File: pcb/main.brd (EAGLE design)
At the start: 100 x 80 mm, 1 part

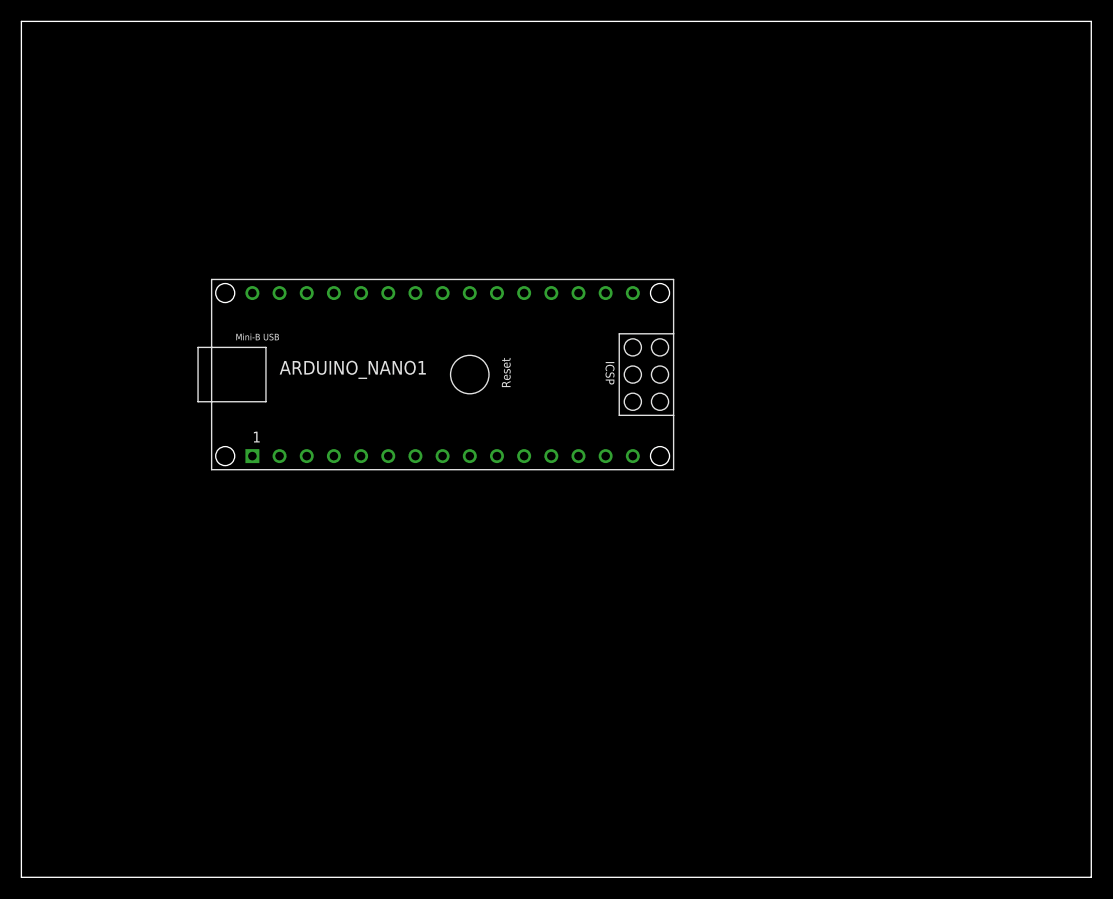
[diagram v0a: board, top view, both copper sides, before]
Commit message: Added PCD8544 symbol and device
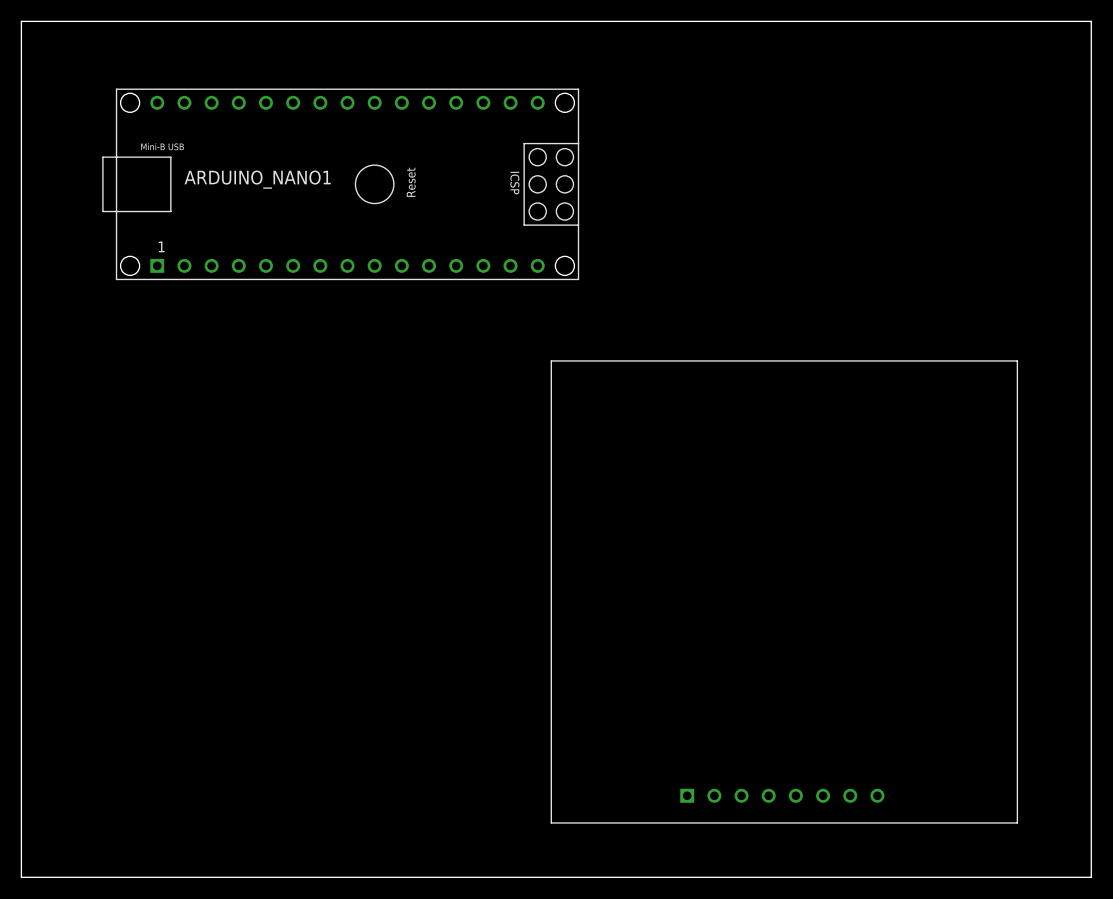
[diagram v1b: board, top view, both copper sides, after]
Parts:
- added DISP1: PCD8544, PCD8544:PCD8544_BTM
- moved ARDUINO_NANO1 19.9 mm to (33.0, 64.8)
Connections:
- new net VCC: DISP1.6
- net GND: now also DISP1.8
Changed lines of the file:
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@@
 </autorouter>
 <elements>
-<element name="ARDUINO_NANO1" library="ArduinoNanoV30" package="ARDUINO_NANO" value="" x="41.91" y="46.99" smashed="yes">
-<attribute name="NAME" x="24.13" y="46.99" size="1.27" layer="21" font="vector"/>
-<attribute name="VALUE" x="24.13" y="44.45" size="1.27" layer="21" font="vector"/>
+<element name="ARDUINO_NANO1" library="ArduinoNanoV30" package="ARDUINO_NANO" value="" x="33.02" y="64.77" smashed="yes">
+<attribute name="NAME" x="15.24" y="64.77" size="1.27" layer="21" font="vector"/>
+<attribute name="VALUE" x="15.24" y="62.23" size="1.27" layer="21" font="vector"/>
 </element>
+<element name="DISP1" library="PCD8544" package="PCD8544_BTM" value="PCD8544" x="69.85" y="3.81" smashed="yes"/>
 </elements>
 <signals>
@@
 <contactref element="ARDUINO_NANO1" pad="19"/>
 <contactref element="ARDUINO_NANO1" pad="14"/>
-<wire x1="54.61" y1="39.37" x2="49.53" y2="54.61" width="0" layer="19" extent="1-1"/>
+<contactref element="DISP1" pad="8"/>
+<wire x1="45.72" y1="57.15" x2="40.64" y2="72.39" width="0" layer="19" extent="1-1"/>
+<wire x1="80.01" y1="7.62" x2="45.72" y2="57.15" width="0" layer="19" extent="1-1"/>
 </signal>
 <signal name="5V">
@@
 <contactref element="ARDUINO_NANO1" pad="15"/>
 </signal>
+<signal name="VCC">
+<contactref element="DISP1" pad="6"/>
+</signal>
 </signals>
